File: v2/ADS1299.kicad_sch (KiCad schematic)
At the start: 49 parts, among them U1 ADS1299IPAGR, U3 TPD4E1B06DCKR, U4 TPD4E1B06DCKR, U9 TPD4E1B06DCKR

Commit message: fix bias
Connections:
- net Bias: no longer U1.62 (BIASIN), U1.63 (BIASOUT)
- net at C1.1, R1.1: now also U1.62 (BIASIN), U1.63 (BIASOUT); no longer U1.61 (BIASINV)
- no-connect marks 0 -> 1
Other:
- moved on the sheet: C1, R1
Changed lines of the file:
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@@
 	)
 	(junction
-		(at 175.26 34.29)
+		(at 170.18 34.29)
 		(diameter 0)
 		(color 0 0 0 0)
@@
 	)
 	(junction
-		(at 185.42 34.29)
+		(at 180.34 34.29)
 		(diameter 0)
 		(color 0 0 0 0)
@@
 	)
 	(junction
-		(at 175.26 38.1)
-		(diameter 0)
-		(color 0 0 0 0)
-	)
-	(junction
 		(at 67.31 156.21)
 		(diameter 0)
@@
 		(color 0 0 0 0)
 	)
+	(no_connect
+		(at 185.42 38.1)
+	)
 	(wire
 		(pts
@@
 	(wire
 		(pts
-			(xy 175.26 25.4) (xy 176.53 25.4)
+			(xy 170.18 25.4) (xy 171.45 25.4)
 		)
 		(stroke
@@
 	(wire
 		(pts
-			(xy 185.42 25.4) (xy 184.15 25.4)
+			(xy 180.34 25.4) (xy 179.07 25.4)
 		)
 		(stroke
@@
 	(wire
 		(pts
-			(xy 185.42 25.4) (xy 185.42 34.29)
+			(xy 180.34 25.4) (xy 180.34 34.29)
 		)
 		(stroke
@@
 	(wire
 		(pts
-			(xy 185.42 34.29) (xy 185.42 38.1)
+			(xy 180.34 34.29) (xy 180.34 38.1)
 		)
 		(stroke
@@
 	(wire
 		(pts
-			(xy 175.26 25.4) (xy 175.26 34.29)
+			(xy 170.18 25.4) (xy 170.18 34.29)
 		)
 		(stroke
@@
 	(wire
 		(pts
-			(xy 165.1 38.1) (xy 175.26 38.1)
+			(xy 165.1 38.1) (xy 170.18 38.1)
 		)
 		(stroke
@@
 	(wire
 		(pts
-			(xy 175.26 38.1) (xy 180.34 38.1)
-		)
-		(stroke
-			(width 0)
-			(type default)
-		)
-	)
-	(wire
-		(pts
 			(xy 67.31 39.37) (xy 67.31 52.07)
 		)
@@
 	(wire
 		(pts
-			(xy 185.42 34.29) (xy 184.15 34.29)
+			(xy 180.34 34.29) (xy 179.07 34.29)
 		)
 		(stroke
@@
 	(wire
 		(pts
-			(xy 175.26 34.29) (xy 176.53 34.29)
+			(xy 170.18 34.29) (xy 171.45 34.29)
 		)
 		(stroke
@@
 	(wire
 		(pts
-			(xy 175.26 34.29) (xy 175.26 38.1)
+			(xy 170.18 34.29) (xy 170.18 38.1)
 		)
 		(stroke
@@
 	(symbol
 		(lib_id "Device:C")
-		(at 180.34 25.4 270)
+		(at 175.26 25.4 270)
 		(unit 1)
 		(exclude_from_sim no)
@@
 		(dnp no)
 		(property "Reference" "C1"
-			(at 180.34 19.558 90)
+			(at 175.26 19.558 90)
 			(effects
 				(font
@@
 		)
 		(property "Value" "1.5nF"
-			(at 180.34 21.844 90)
+			(at 175.26 21.844 90)
 			(effects
 				(font
@@
 		)
 		(property "Footprint" "Capacitor_SMD:C_0805_2012Metric_Pad1.18x1.45mm_HandSolder"
-			(at 176.53 26.3652 0)
+			(at 171.45 26.3652 0)
 			(effects
 				(font
@@
 		)
 		(property "Datasheet" "~"
-			(at 180.34 25.4 0)
+			(at 175.26 25.4 0)
 			(effects
 				(font
@@
 		)
 		(property "Description" "Unpolarized capacitor"
-			(at 180.34 25.4 0)
+			(at 175.26 25.4 0)
 			(effects
 				(font
@@
 	(symbol
 		(lib_id "Device:R")
-		(at 180.34 34.29 270)
+		(at 175.26 34.29 270)
 		(unit 1)
 		(exclude_from_sim no)
@@
 		(dnp no)
 		(property "Reference" "R1"
-			(at 180.34 29.972 90)
+			(at 175.26 29.972 90)
 			(effects
 				(font
@@
 		)
 		(property "Value" "1MΩ"
-			(at 180.34 31.75 90)
+			(at 175.26 31.75 90)
 			(effects
 				(font
@@
 		)
 		(property "Footprint" "Resistor_SMD:R_0402_1005Metric_Pad0.72x0.64mm_HandSolder"
-			(at 180.34 32.512 90)
+			(at 175.26 32.512 90)
 			(effects
 				(font
@@
 		)
 		(property "Datasheet" "~"
-			(at 180.34 34.29 0)
+			(at 175.26 34.29 0)
 			(effects
 				(font
@@
 		)
 		(property "Description" "Resistor"
-			(at 180.34 34.29 0)
+			(at 175.26 34.29 0)
 			(effects
 				(font

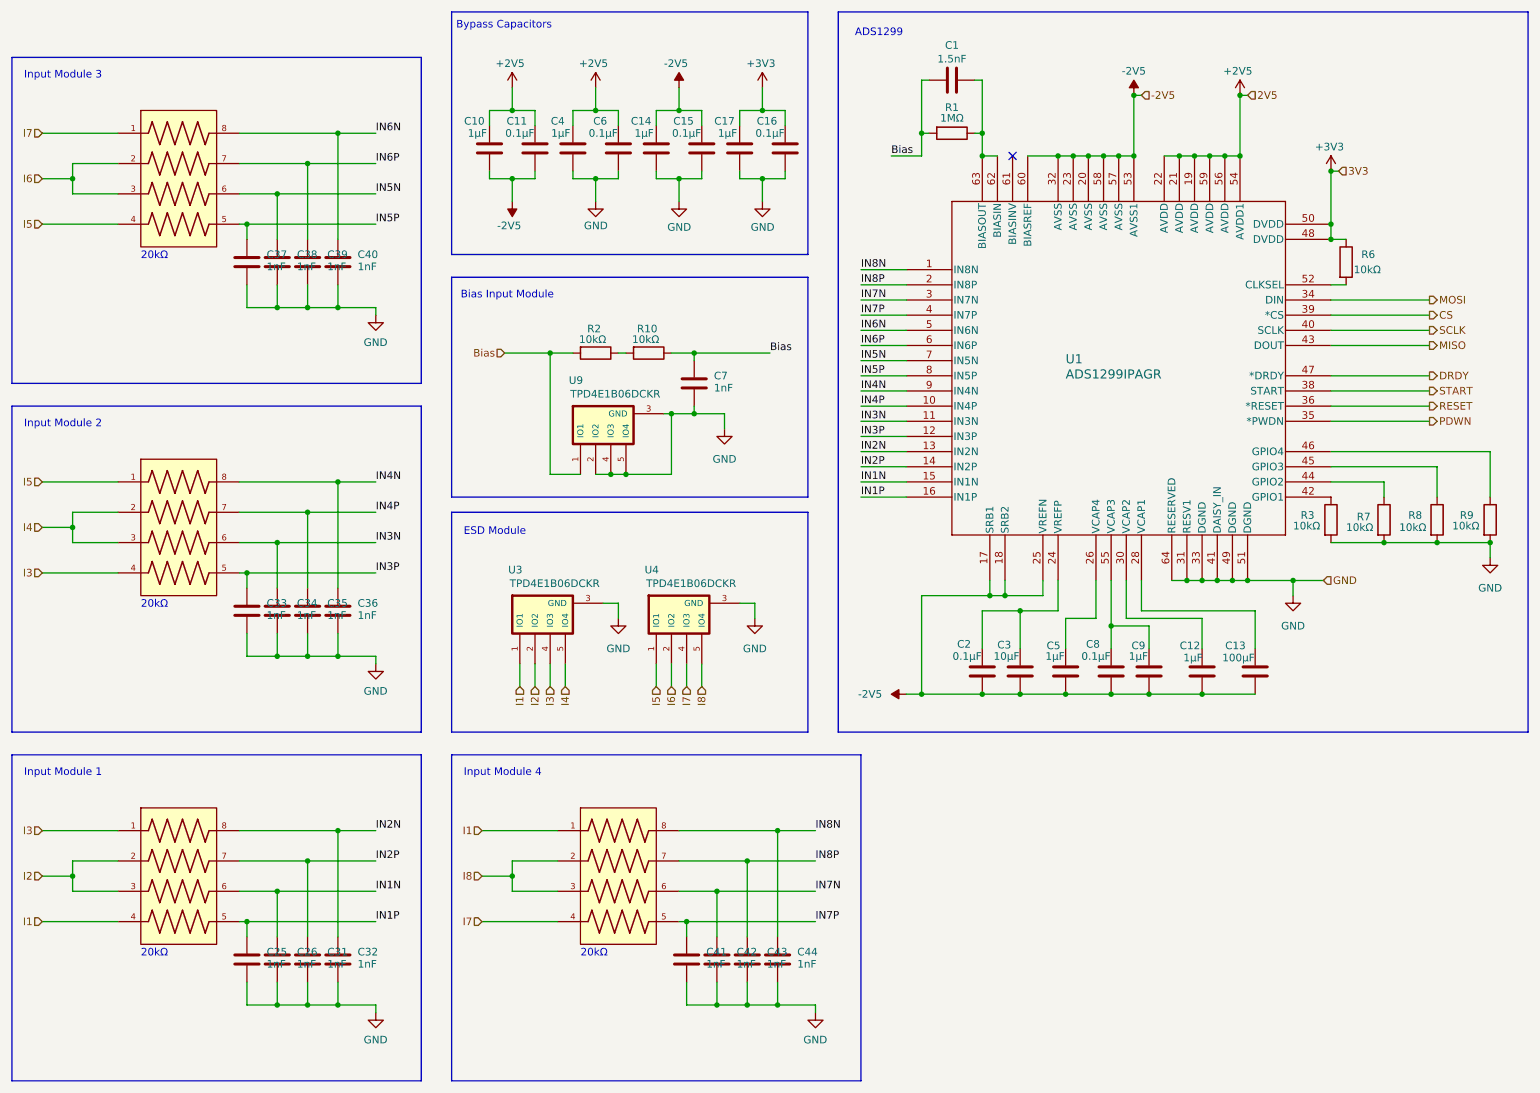
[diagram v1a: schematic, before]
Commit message: footprint reset for v0.2
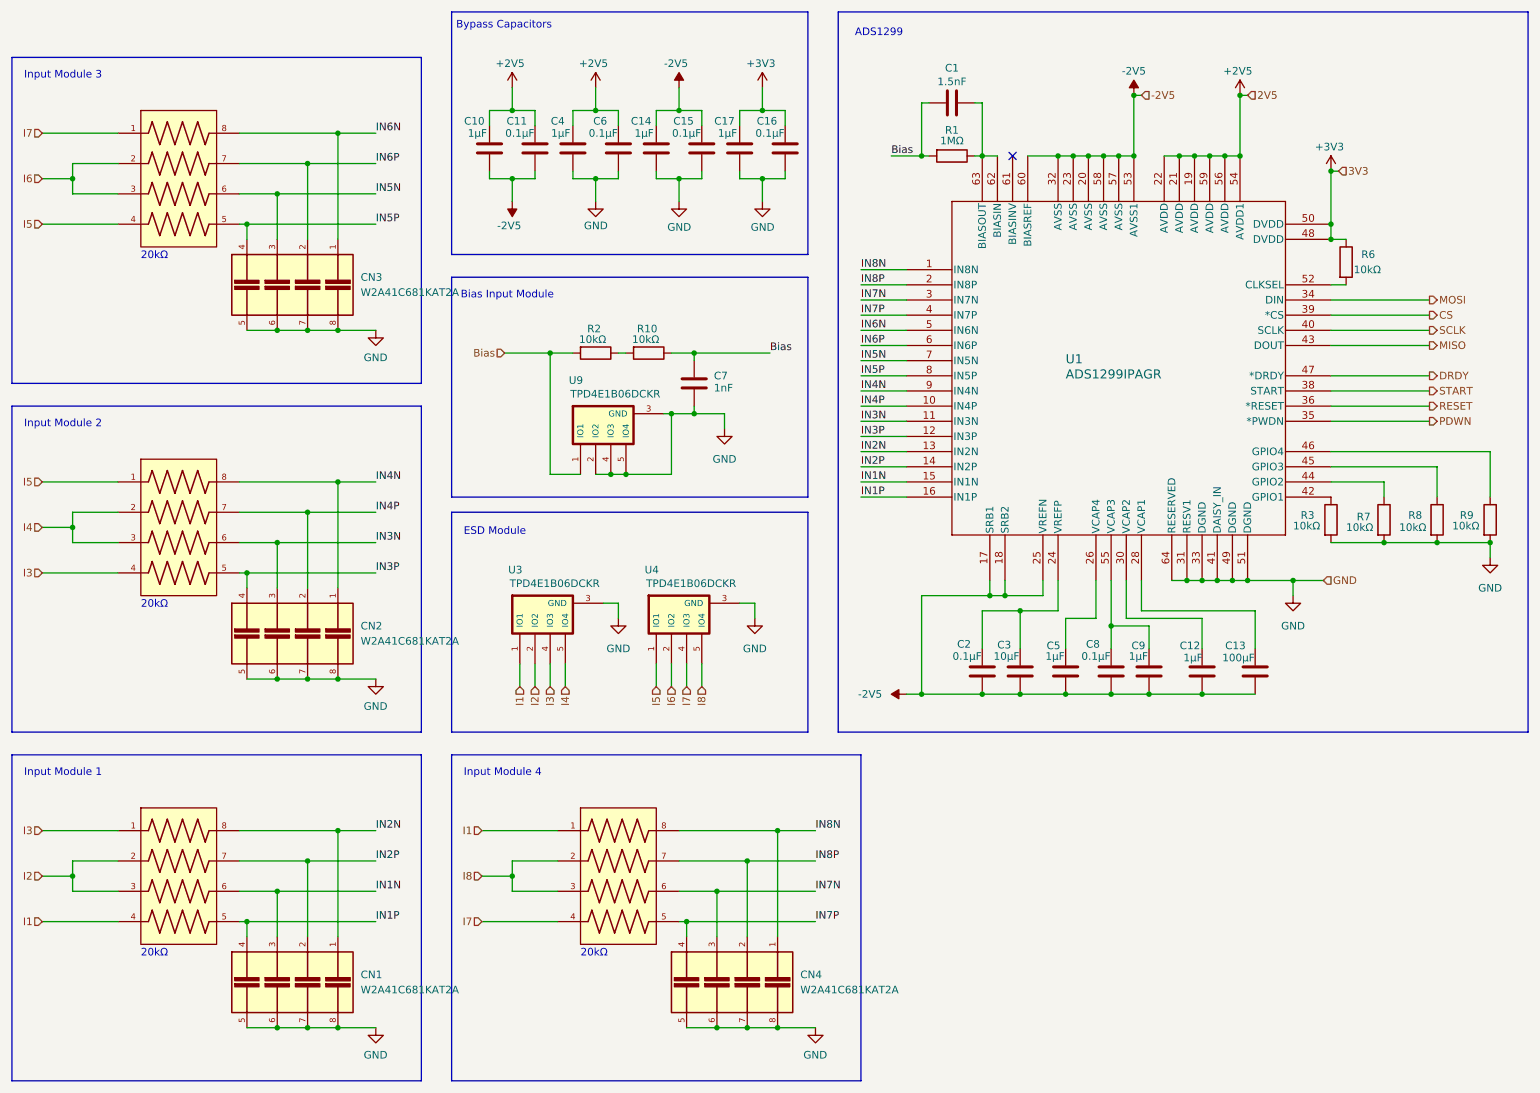
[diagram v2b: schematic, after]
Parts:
- removed C25, C26, C31, C32, C33, C34, C35, C36, C37, C38, C39, C40, C41, C42, C43, C44: 1nF, Capacitor_SMD:C_0603_1608Metric_Pad1.08x0.95mm_HandSolder, symbol Device:C
- added CN1, CN2, CN3, CN4: W2A41C681KAT2A, CustomLib:CAP-ARRAY-SMD_6124-8P-L3.2-W1.6-BL, symbol custom_lib:W2A41C681KAT2A
- C1, C3: footprint Capacitor_SMD:C_0805_2012Metric_Pad1.18x1.45mm_HandSolder -> (none)
- C10, C12, C14, C17, C4, C5, C9: footprint Capacitor_SMD:C_0402_1005Metric_Pad0.74x0.62mm_HandSolder -> (none)
- C11, C15, C16, C2, C6, C7, C8: footprint Capacitor_SMD:C_0603_1608Metric_Pad1.08x0.95mm_HandSolder -> (none)
- C13: footprint Capacitor_SMD:C_1210_3225Metric_Pad1.33x2.70mm_HandSolder -> (none)
- R1: footprint Resistor_SMD:R_0402_1005Metric_Pad0.72x0.64mm_HandSolder -> (none)
- R10, R2, R3, R6, R7, R8, R9: footprint Resistor_SMD:R_0805_2012Metric_Pad1.20x1.40mm_HandSolder -> (none)
- RN5, RN6, RN7, RN8: footprint CustomLib:CAT16A203J4LF -> CustomLib:RES-ARRAY-SMD_0603-8P-L3.2-W1.6-BL
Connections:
- net GND: now also CN1.5, CN1.6, CN1.7, CN1.8, CN2.5, CN2.6, CN2.7, CN2.8, CN3.5, CN3.6, CN3.7, CN3.8, CN4.5, CN4.6, CN4.7, CN4.8
- net IN1N: now also CN1.3
- net IN1P: now also CN1.4
- net IN2N: now also CN1.1
- net IN2P: now also CN1.2
- net IN3N: now also CN2.3
- net IN3P: now also CN2.4
- net IN4N: now also CN2.1
- net IN4P: now also CN2.2
- net IN5N: now also CN3.3
- net IN5P: now also CN3.4
- net IN6N: now also CN3.1
- net IN6P: now also CN3.2
- net IN7N: now also CN4.3
- net IN7P: now also CN4.4
- net IN8N: now also CN4.1
- net IN8P: now also CN4.2
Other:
- moved on the sheet: C1, R1

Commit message: new footprints
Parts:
- C1, C10, C11, C12, C14, C15, C16, C17, C2, C3, C4, C5, C6, C7, C8, C9: footprint (none) -> Capacitor_SMD:C_0603_1608Metric_Pad1.08x0.95mm_HandSolder
- C13: footprint (none) -> Capacitor_SMD:C_1206_3216Metric_Pad1.33x1.80mm_HandSolder
- R1, R10, R2, R3, R6, R7, R8, R9: footprint (none) -> Resistor_SMD:R_0603_1608Metric_Pad0.98x0.95mm_HandSolder
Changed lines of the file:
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@@
 			)
 		)
-		(property "Footprint" ""
+		(property "Footprint" "Resistor_SMD:R_0603_1608Metric_Pad0.98x0.95mm_HandSolder"
 			(at 124.46 69.342 90)
 			(effects
@@
 			)
 		)
-		(property "Footprint" ""
+		(property "Footprint" "Capacitor_SMD:C_0603_1608Metric_Pad1.08x0.95mm_HandSolder"
 			(at 179.3748 120.65 0)
 			(effects
@@
 			)
 		)
-		(property "Footprint" ""
+		(property "Footprint" "Resistor_SMD:R_0603_1608Metric_Pad0.98x0.95mm_HandSolder"
 			(at 263.652 99.06 90)
 			(effects
@@
 			)
 		)
-		(property "Footprint" ""
+		(property "Footprint" "Capacitor_SMD:C_1206_3216Metric_Pad1.33x1.80mm_HandSolder"
 			(at 227.0252 128.27 0)
 			(effects
@@
 			)
 		)
-		(property "Footprint" ""
+		(property "Footprint" "Resistor_SMD:R_0603_1608Metric_Pad0.98x0.95mm_HandSolder"
 			(at 245.872 99.06 90)
 			(effects
@@
 			)
 		)
-		(property "Footprint" ""
+		(property "Footprint" "Capacitor_SMD:C_0603_1608Metric_Pad1.08x0.95mm_HandSolder"
 			(at 200.9648 120.65 0)
 			(effects
@@
 			)
 		)
-		(property "Footprint" ""
+		(property "Footprint" "Resistor_SMD:R_0603_1608Metric_Pad0.98x0.95mm_HandSolder"
 			(at 239.522 55.88 90)
 			(effects
@@
 			)
 		)
-		(property "Footprint" ""
+		(property "Footprint" "Resistor_SMD:R_0603_1608Metric_Pad0.98x0.95mm_HandSolder"
 			(at 236.982 99.06 90)
 			(effects
@@
 			)
 		)
-		(property "Footprint" ""
+		(property "Footprint" "Capacitor_SMD:C_0603_1608Metric_Pad1.08x0.95mm_HandSolder"
 			(at 134.3152 40.64 0)
 			(effects
@@
 			)
 		)
-		(property "Footprint" ""
+		(property "Footprint" "Capacitor_SMD:C_0603_1608Metric_Pad1.08x0.95mm_HandSolder"
 			(at 98.7552 40.64 0)
 			(effects
@@
 			)
 		)
-		(property "Footprint" ""
+		(property "Footprint" "Capacitor_SMD:C_0603_1608Metric_Pad1.08x0.95mm_HandSolder"
 			(at 133.0452 80.01 0)
 			(effects
@@
 			)
 		)
-		(property "Footprint" ""
+		(property "Footprint" "Capacitor_SMD:C_0603_1608Metric_Pad1.08x0.95mm_HandSolder"
 			(at 207.3148 120.65 0)
 			(effects
@@
 			)
 		)
-		(property "Footprint" ""
+		(property "Footprint" "Capacitor_SMD:C_0603_1608Metric_Pad1.08x0.95mm_HandSolder"
 			(at 112.7252 40.64 0)
 			(effects
@@
 			)
 		)
-		(property "Footprint" ""
+		(property "Footprint" "Capacitor_SMD:C_0603_1608Metric_Pad1.08x0.95mm_HandSolder"
 			(at 218.1352 128.27 0)
 			(effects
@@
 			)
 		)
-		(property "Footprint" ""
+		(property "Footprint" "Resistor_SMD:R_0603_1608Metric_Pad0.98x0.95mm_HandSolder"
 			(at 115.57 69.342 90)
 			(effects
@@
 			)
 		)
-		(property "Footprint" ""
+		(property "Footprint" "Capacitor_SMD:C_0603_1608Metric_Pad1.08x0.95mm_HandSolder"
 			(at 171.45 30.1752 0)
 			(effects
@@
 			)
 		)
-		(property "Footprint" ""
+		(property "Footprint" "Resistor_SMD:R_0603_1608Metric_Pad0.98x0.95mm_HandSolder"
 			(at 175.26 36.322 90)
 			(effects
@@
 			)
 		)
-		(property "Footprint" ""
+		(property "Footprint" "Resistor_SMD:R_0603_1608Metric_Pad0.98x0.95mm_HandSolder"
 			(at 254.762 99.06 90)
 			(effects
@@
 			)
 		)
-		(property "Footprint" ""
+		(property "Footprint" "Capacitor_SMD:C_0603_1608Metric_Pad1.08x0.95mm_HandSolder"
 			(at 187.6552 128.27 0)
 			(effects
@@
 			)
 		)
-		(property "Footprint" ""
+		(property "Footprint" "Capacitor_SMD:C_0603_1608Metric_Pad1.08x0.95mm_HandSolder"
 			(at 120.3452 40.64 0)
 			(effects
@@
 			)
 		)
-		(property "Footprint" ""
+		(property "Footprint" "Capacitor_SMD:C_0603_1608Metric_Pad1.08x0.95mm_HandSolder"
 			(at 106.3752 40.64 0)
 			(effects
@@
 			)
 		)
-		(property "Footprint" ""
+		(property "Footprint" "Capacitor_SMD:C_0603_1608Metric_Pad1.08x0.95mm_HandSolder"
 			(at 140.6652 40.64 0)
 			(effects
@@
 			)
 		)
-		(property "Footprint" ""
+		(property "Footprint" "Capacitor_SMD:C_0603_1608Metric_Pad1.08x0.95mm_HandSolder"
 			(at 148.2852 40.64 0)
 			(effects
@@
 			)
 		)
-		(property "Footprint" ""
+		(property "Footprint" "Capacitor_SMD:C_0603_1608Metric_Pad1.08x0.95mm_HandSolder"
 			(at 126.6952 40.64 0)
 			(effects
@@
 			)
 		)
-		(property "Footprint" ""
+		(property "Footprint" "Capacitor_SMD:C_0603_1608Metric_Pad1.08x0.95mm_HandSolder"
 			(at 195.2752 128.27 0)
 			(effects
